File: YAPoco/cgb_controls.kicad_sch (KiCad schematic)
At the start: 8 parts, among them SW2 Right, SW3 Down, SW4 Up, SW5 Left, SW6 A, SW7 B, SW8 Select, SW9 Start

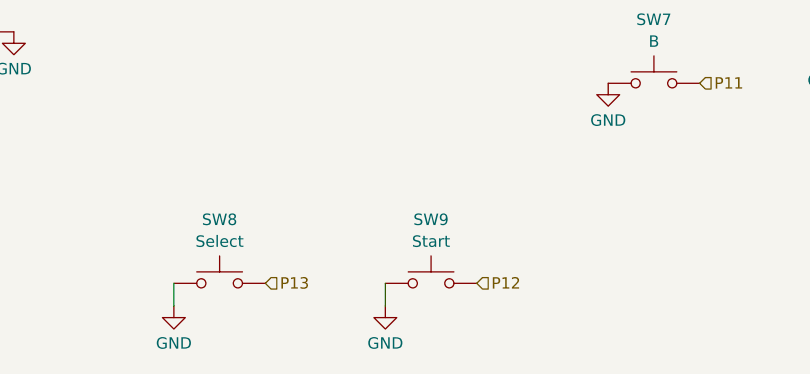
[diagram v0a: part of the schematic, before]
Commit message: updated some labels
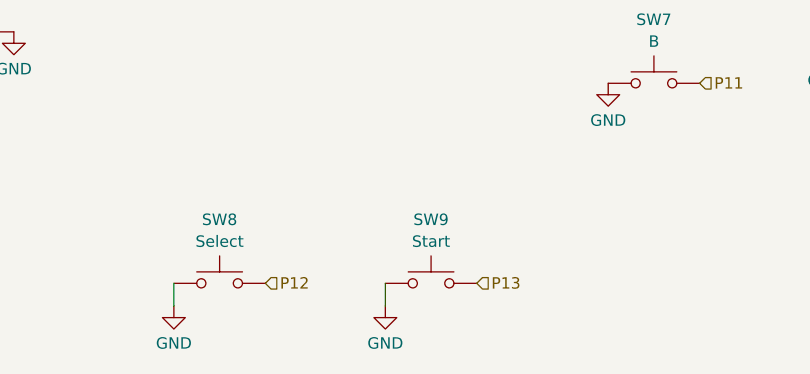
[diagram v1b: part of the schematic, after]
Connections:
- net P12: now also SW8.2; no longer SW9.2
- net P13: now also SW9.2; no longer SW8.2
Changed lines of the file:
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@@
 		)
 	)
-	(hierarchical_label "P13"
+	(hierarchical_label "P12"
 		(shape input)
 		(at 97.79 109.855 0)
@@
 		)
 	)
-	(hierarchical_label "P12"
+	(hierarchical_label "P10"
 		(shape input)
-		(at 121.285 109.855 0)
+		(at 170.18 83.185 0)
 		(fields_autoplaced yes)
 		(effects
@@
 		)
 	)
-	(hierarchical_label "P10"
+	(hierarchical_label "P13"
 		(shape input)
-		(at 170.18 83.185 0)
+		(at 121.285 109.855 0)
 		(fields_autoplaced yes)
 		(effects
